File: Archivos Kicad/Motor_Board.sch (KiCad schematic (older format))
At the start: 63 parts, among them IC1 L298, P1 CONN_2_V, P2 CONN_2_V, P3 CONN_2_V, SW1 SWITCH_INV, U2 7805

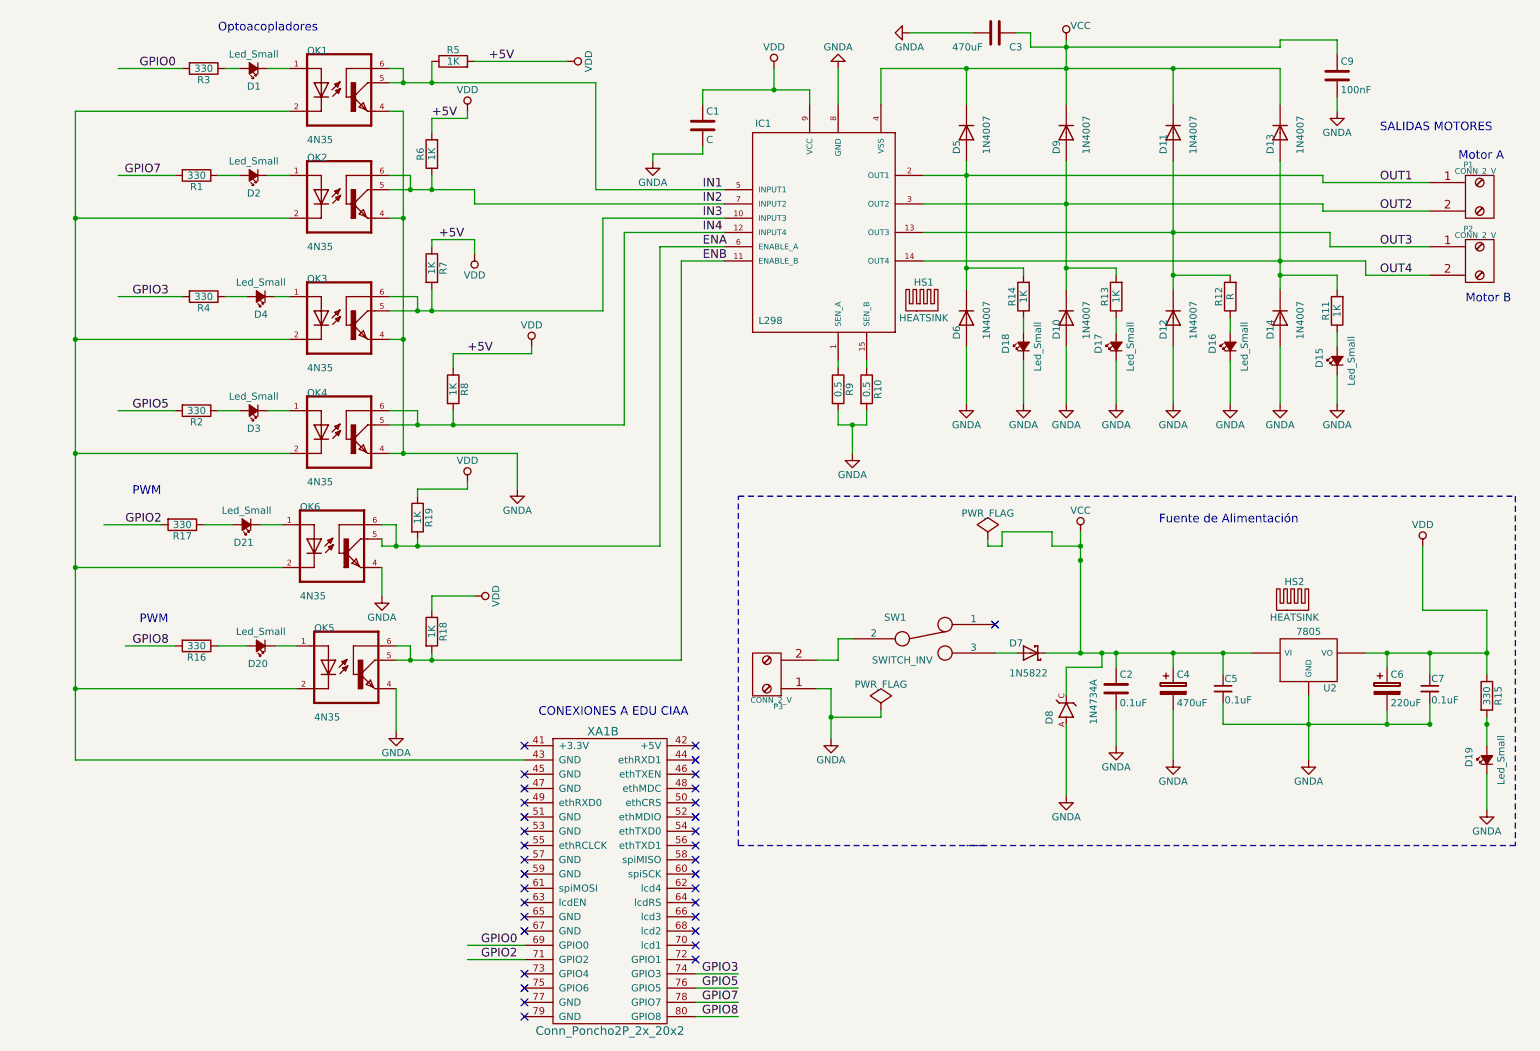
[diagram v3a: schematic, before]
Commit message: Esquemático con los campos de digikey y mouser para hacer andar Kicost.
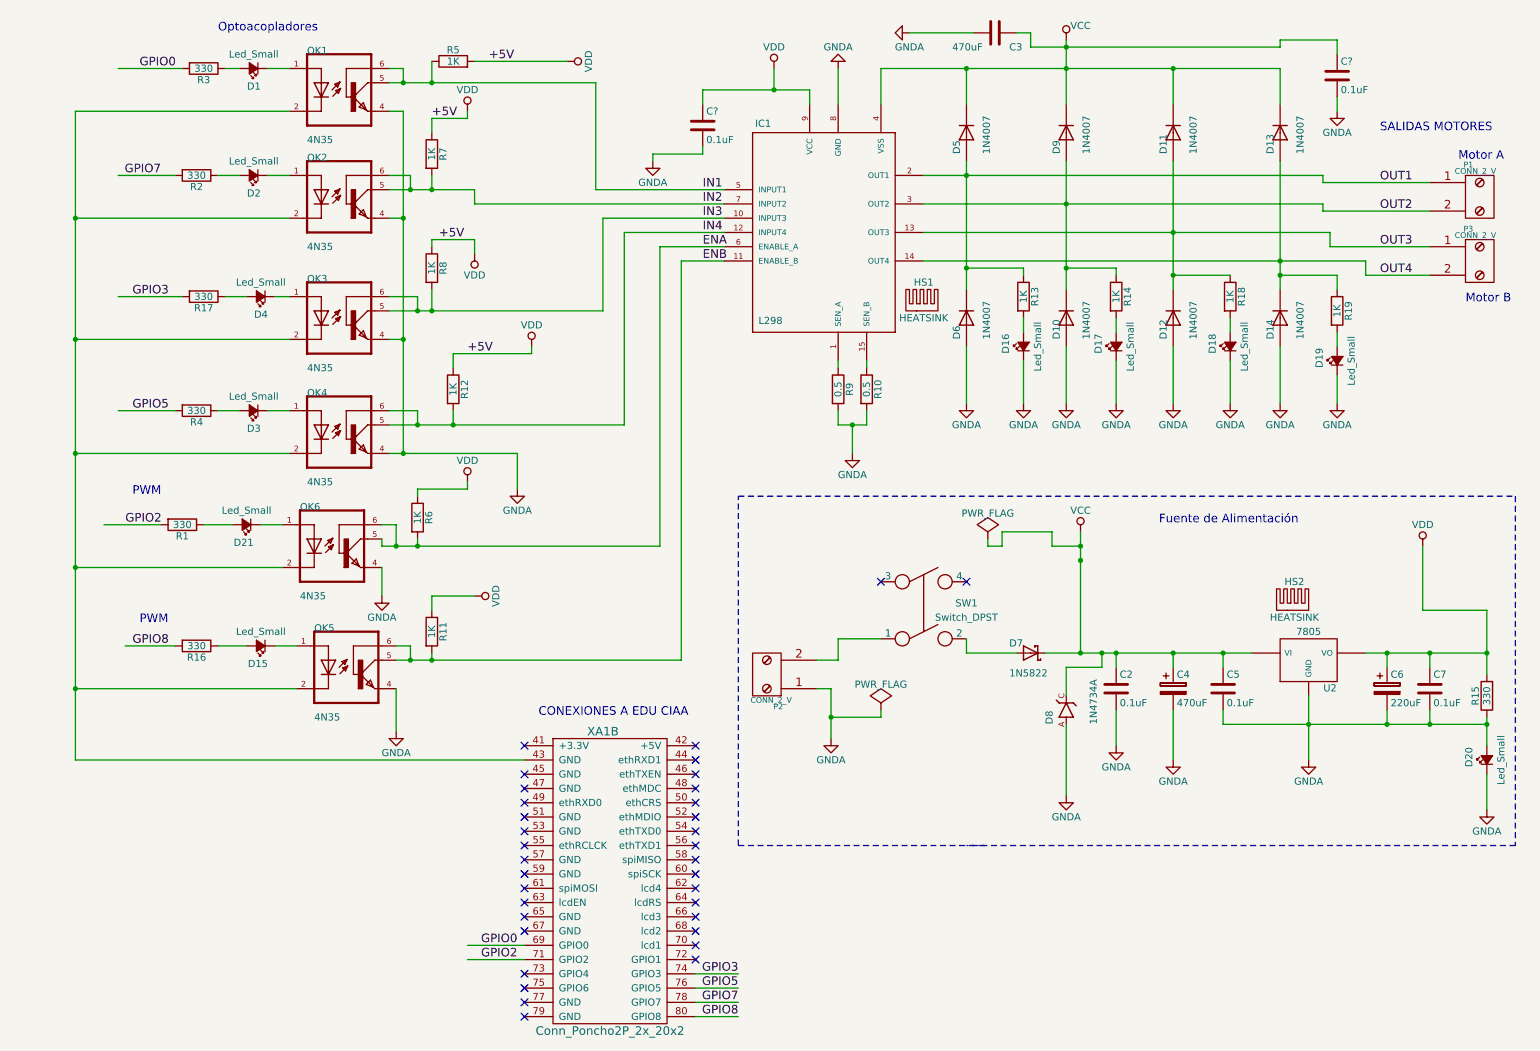
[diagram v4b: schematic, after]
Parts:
- removed C1: C, symbol C
- removed C5, C7: 0.1uF, symbol C_Small
- removed C9: 100nF, symbol C
- removed SW1: SWITCH_INV, symbol SWITCH_INV
- added C5, C7, C? (x2): 0.1uF, symbol C
- added SW1: Switch_DPST, symbol Switch_DPST
- C2: Digikey# Value -> 445-173145-3-ND; Manf Value -> TDK; Manf# Value -> FG16C0G1H104JNT06; Mouser# (none) -> 810-FG16C0G1H104JNT6
- C3: Digikey# Value -> 565-3264-ND; Manf Value -> United Chemi-Con; Manf# Value -> KHD160E477M90C0B00; Mouser# (none) -> Value
- C4: Digikey# Value -> P5185-ND; Manf Value -> Panasonic; Manf# Value -> ECA-1HM471; Mouser# (none) -> 667-ECA-1HM471
- C6: Digikey# Value -> P12397-ND; Manf Value -> Panasonic; Manf# Value -> EEU-FM1H221; Mouser# (none) -> 667-EEU-FM1H221
- D1, D15, D16, D17, D18, D19, D2, D20, D21, D3, D4: Digikey# (none) -> 516-1331-ND; LibPart (none) -> Value; Manf (none) -> Broadcom Limited; Manf# (none) -> HLMP-3401; Mouser# (none) -> 630-HLMP-3401
- D10, D11, D12, D13, D14, D5, D6, D9: Digikey# (none) -> 1N4007FSCT-ND; LibPart (none) -> Value; Manf (none) -> Fairchild Semiconductor; Manf# (none) -> 1N4007; Mouser# (none) -> 512-1N4007
- D7: Digikey# (none) -> 497-11370-3-ND; LibPart (none) -> Value; Manf (none) -> STMicroelectronics; Manf# (none) -> 1N5822; Mouser# (none) -> 511-1N5822
- D8: Digikey# (none) -> 1N4734AFS-ND; LibPart (none) -> Value; Manf (none) -> Fairchild Semiconductor; Manf# (none) -> 1N4734A; Mouser# (none) -> 512-1N4734A
- IC1: Digikey# (none) -> 497-1395-5-ND; LibPart (none) -> Value; Manf (none) -> STMicroelectronics; Manf# (none) -> L298N; Mouser# (none) -> 511-L298
- OK1, OK2, OK3, OK4, OK5, OK6: Digikey# (none) -> 4N35-ND; LibPart (none) -> Value; Manf (none) -> Vishay Semiconductor Opto Division; Manf# (none) -> 4N35; Mouser# (none) -> 78-4N35
- P1, P2, P3: Digikey# (none) -> WM13976-ND; LibPart (none) -> Value; Manf (none) -> Molex, LLC; Manf# (none) -> 0398890042; Mouser# (none) -> 538-39889-0042
- R1, R15, R16, R17, R2, R3, R4: Digikey# Value -> 330QBK-ND; Manf Value -> Yageo; Manf# Value -> CFR-25JR-52-330R; Mouser# (none) -> 603-CFR-25JR-52330R
- R10: Digikey# Value -> 55JR50E-ND; Manf Value -> Ohmite; Manf# Value -> 55JR50E; Mouser# (none) -> 55JR50E; POWER 3W -> (none); Power (none) -> 5W
- R11, R13, R14, R18, R19, R5, R6, R7, R8: footprint (none) -> ~; Digikey# Value -> 1.0KQTR-ND; Manf Value -> Yageo; Manf# Value -> CFR-25JR-52-1K; Mouser# (none) -> 603-CFR-25JB-1K0
- R12: value R -> 1K; footprint (none) -> ~; Digikey# (none) -> 1.0KQTR-ND; LibPart (none) -> Value; Manf (none) -> Yageo; Manf# (none) -> CFR-25JR-52-1K; Mouser# (none) -> 603-CFR-25JB-1K0
- R9: Digikey# Value -> 55JR50E-ND; Manf Value -> Ohmite; Manf# Value -> 55JR50E; Mouser# (none) -> 55JR50E; Power 3W -> 5W
- U2: Digikey# (none) -> 497-12404-ND; LibPart (none) -> Value; Manf (none) -> STMicroelectronics; Manf# (none) -> L7805CV-DG; Mouser# (none) -> 511-L7805CV
- XA1: Digikey# (none) -> S6104-ND; LibPart (none) -> Value; Manf (none) -> Sullins Connector Solutions; Manf# (none) -> PPTC202LFBN-RC; Mouser# (none) -> Value
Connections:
- wire segments 193 -> 194
- no-connect marks 34 -> 35

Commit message: Cambios realizados al esquemático y primeros pasos del PCB.
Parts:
- removed HS1, HS2: HEATSINK, symbol HEATSINK
- removed SW1: Switch_DPST, symbol Switch_DPST
- added D22: Led_Small, Motor_Board:LED-3MM, symbol Led_Small
- added F1, F2, F3: FIDUCIAL, Motor_Board:Fiducial_1mm, symbol FIDUCIAL
- added R20: 1K, Motor_Board:Resistor_Horizontal_RM10mm, symbol R
- added SW1: Switch_SPDT_x2, Motor_Board:SW_Micro_SPST, symbol Switch_SPDT_x2
- C1, C8: renamed from C?; footprint (none) -> Motor_Board:C_Disc_D3_P2.5
- C2, C5, C7: footprint (none) -> Motor_Board:C_Disc_D3_P2.5
- C3, C4: footprint (none) -> Motor_Board:C_Radial_D10_L25_P5
- C6: footprint (none) -> Motor_Board:C_Radial_D10_L16_P5
- D1, D15, D16, D17, D18, D19, D2, D20, D21, D3, D4: footprint (none) -> Motor_Board:LED-3MM
- D10, D11, D12, D13, D14, D5, D6, D9: footprint DIOAD1070W78L465D235P -> Motor_Board:Diode_DO-41_SOD81_Horizontal_RM10
- D7: footprint DIOAD2120W130L950D530P -> Motor_Board:Diode_DO-201AD_Horizontal_RM15
- D8: footprint DIOAD1070W78L463D238P -> Motor_Board:Diode_DO-35_SOD27_Horizontal_RM10
- IC1: footprint stepper drivers-MW-15 -> Motor_Board:Multiwatt_15_Vertical
- OK1, OK2, OK3, OK4, OK5, OK6: footprint DIL06 -> Motor_Board:DIP-6_W7.62mm
- P1: value CONN_2_V -> Motor A; footprint (none) -> Motor_Board:bornier2
- P2: value CONN_2_V -> VDD Motor; footprint (none) -> Motor_Board:bornier2
- P3: value CONN_2_V -> Motor B; footprint (none) -> Motor_Board:bornier2
- R1, R15, R16, R17, R2, R3, R4: footprint (none) -> Motor_Board:Resistor_Horizontal_RM10mm
- R10, R9: footprint (none) -> Motor_Board:Resistor_Ceramic_Horizontal_L19mm-W8mm-H8mm-p25mm
- R11, R12, R13, R14, R18, R19, R5, R6, R7, R8: footprint ~ -> Motor_Board:Resistor_Horizontal_RM10mm
- U2: footprint (none) -> Motor_Board:TO-220
- XA1: footprint (none) -> Motor_Board:Conn_Poncho_Izquierda; Digikey# S6104-ND -> 3M1440-ND; Manf Sullins Connector Solutions -> 3M; Manf# PPTC202LFBN-RC -> 151240-8422-RB; Mouser# Value -> 517-151240-8422-RB
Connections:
- wire segments 194 -> 199
- no-connect marks 35 -> 34
